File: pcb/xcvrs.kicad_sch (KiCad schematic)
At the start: 6 parts, among them U6 TCAN3403-Q1

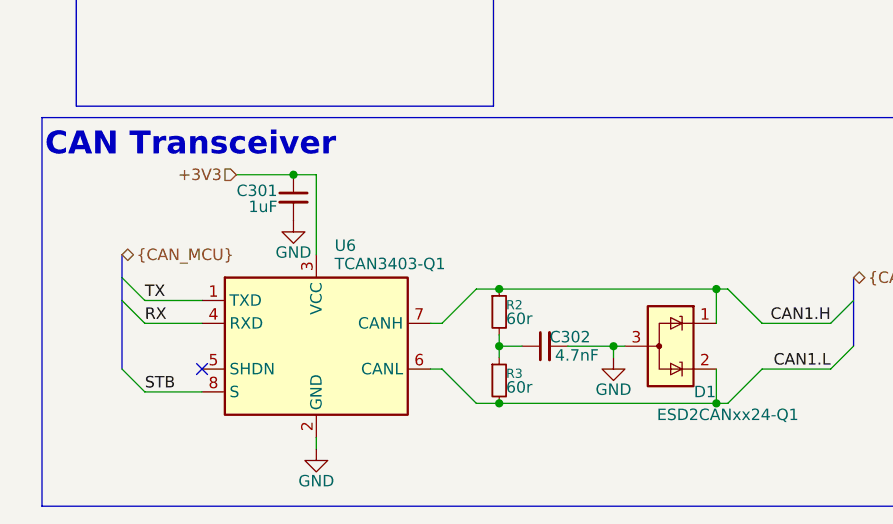
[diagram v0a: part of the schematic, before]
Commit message: pcb gitignore update, netting and mcu pinning
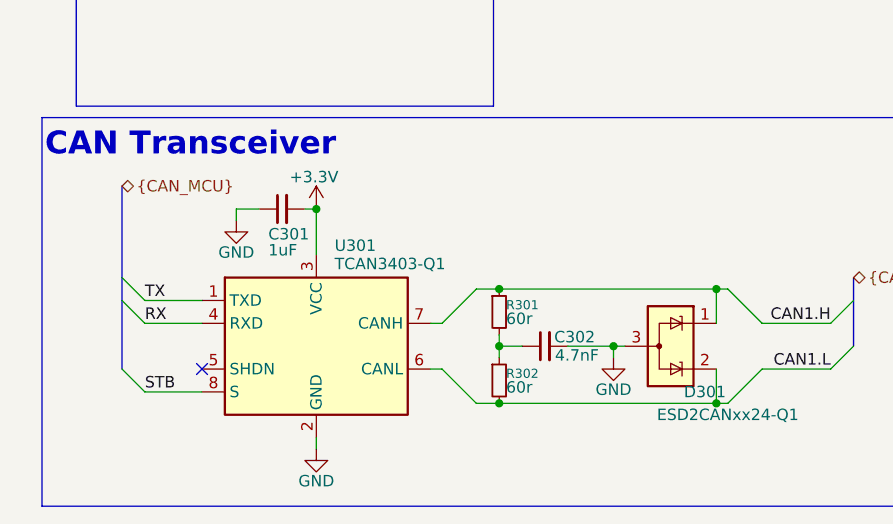
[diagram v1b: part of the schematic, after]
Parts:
- C301: footprint (none) -> Capacitor_SMD:C_0402_1005Metric
- R301: renamed from R2; footprint (none) -> Resistor_SMD:R_0402_1005Metric
- R302: renamed from R3; footprint (none) -> Resistor_SMD:R_0402_1005Metric
- renumbered D1 to D301, U6 to U301
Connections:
- net GND: now also C301.1; no longer C301.2
- net +3V3 renamed +3.3V
- net +3.3V: now also C301.2; no longer C301.1
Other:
- moved on the sheet: C301
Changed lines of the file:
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@@
+	)
+	(junction
+		(at 46.99 82.55)
+		(diameter 0)
+		(color 0 0 0 0)
 	)
 	(junction
@@
 	)
 	(junction
-		(at 44.45 78.74)
-		(diameter 0)
-		(color 0 0 0 0)
-	)
-	(junction
 		(at 80.01 97.79)
 		(diameter 0)
@@
 	(wire
 		(pts
-			(xy 46.99 78.74) (xy 46.99 87.63)
-		)
-		(stroke
-			(width 0)
-			(type default)
-		)
-	)
-	(wire
-		(pts
 			(xy 88.9 33.02) (xy 100.33 33.02)
 		)
@@
 	(wire
 		(pts
-			(xy 44.45 78.74) (xy 46.99 78.74)
-		)
-		(stroke
-			(width 0)
-			(type default)
-		)
-	)
-	(wire
-		(pts
 			(xy 91.44 91.44) (xy 92.71 91.44)
 		)
@@
 	(wire
 		(pts
+			(xy 46.99 82.55) (xy 46.99 87.63)
+		)
+		(stroke
+			(width 0)
+			(type default)
+		)
+	)
+	(wire
+		(pts
 			(xy 46.99 107.95) (xy 46.99 109.22)
 		)
@@
 	(wire
 		(pts
+			(xy 45.72 82.55) (xy 46.99 82.55)
+		)
+		(stroke
+			(width 0)
+			(type default)
+		)
+	)
+	(wire
+		(pts
 			(xy 105.41 48.26) (xy 81.28 48.26)
 		)
@@
 		)
 	)
+	(wire
+		(pts
+			(xy 38.1 82.55) (xy 40.64 82.55)
+		)
+		(stroke
+			(width 0)
+			(type default)
+		)
+	)
 	(bus
 		(pts
@@
 	(wire
 		(pts
-			(xy 38.1 78.74) (xy 44.45 78.74)
-		)
-		(stroke
-			(width 0)
-			(type default)
-		)
-	)
-	(wire
-		(pts
 			(xy 96.52 95.25) (xy 92.71 91.44)
 		)
@@
 	(wire
 		(pts
+			(xy 38.1 82.55) (xy 38.1 83.82)
+		)
+		(stroke
+			(width 0)
+			(type default)
+		)
+	)
+	(wire
+		(pts
 			(xy 81.28 97.79) (xy 80.01 97.79)
 		)
@@
 	(bus
 		(pts
-			(xy 25.4 87.63) (xy 25.4 90.17)
+			(xy 25.4 80.01) (xy 25.4 90.17)
 		)
 		(stroke
@@
 			)
 			(justify left bottom)
-		)
-	)
-	(hierarchical_label "+3V3"
-		(shape input)
-		(at 38.1 78.74 180)
-		(effects
-			(font
-				(size 1.27 1.27)
-			)
-			(justify right)
 		)
 	)
@@
 	(hierarchical_label "{CAN_MCU}"
 		(shape bidirectional)
-		(at 25.4 87.63 0)
+		(at 25.4 80.01 0)
 		(effects
 			(font
@@
 			)
 			(justify left)
+		)
+	)
+	(symbol
+		(lib_id "power:+BATT")
+		(at 46.99 82.55 0)
+		(unit 1)
+		(exclude_from_sim no)
+		(in_bom yes)
+		(on_board yes)
+		(dnp no)
+		(property "Reference" "#PWR026"
+			(at 46.99 86.36 0)
+			(effects
+				(font
+					(size 1.27 1.27)
+				)
+				(hide yes)
+			)
+		)
+		(property "Value" "+3.3V"
+			(at 46.736 78.994 0)
+			(effects
+				(font
+					(size 1.27 1.27)
+				)
+			)
+		)
+		(property "Footprint" ""
+			(at 46.99 82.55 0)
+			(effects
+				(font
+					(size 1.27 1.27)
+				)
+				(hide yes)
+			)
+		)
+		(property "Datasheet" ""
+			(at 46.99 82.55 0)
+			(effects
+				(font
+					(size 1.27 1.27)
+				)
+				(hide yes)
+			)
+		)
+		(property "Description" "Power symbol creates a global label with name \"+BATT\""
+			(at 46.99 82.55 0)
+			(effects
+				(font
+					(size 1.27 1.27)
+				)
+				(hide yes)
+			)
+		)
+		(pin "1"
+		)
+		(instances
+			(project "kh_obd2_interface"
+				(path "/0736e313-8db4-41af-b70d-53af7104d2ca/5885c24f-1a9e-44c2-aba7-d9491c98e256"
+					(reference "#PWR026")
+					(unit 1)
+				)
+			)
 		)
 	)
@@
 		(dnp no)
 		(property "Reference" "C302"
-			(at 75.184 96.774 90)
+			(at 75.692 96.774 90)
 			(effects
 				(font
@@
 		(on_board yes)
 		(dnp no)
-		(property "Reference" "R3"
+		(property "Reference" "R302"
 			(at 68.072 100.838 0)
 			(effects
@@
 			)
 		)
-		(property "Footprint" ""
+		(property "Footprint" "Resistor_SMD:R_0402_1005Metric"
 			(at 67.31 101.6 0)
 			(effects
@@
 			(project "kh_obd2_interface"
 				(path "/0736e313-8db4-41af-b70d-53af7104d2ca/5885c24f-1a9e-44c2-aba7-d9491c98e256"
-					(reference "R3")
+					(reference "R302")
 					(unit 1)
 				)
@@
 	(symbol
 		(lib_id "power:GND")
-		(at 44.45 83.82 0)
+		(at 38.1 83.82 0)
 		(unit 1)
 		(exclude_from_sim no)
@@
 		(dnp no)
 		(property "Reference" "#PWR011"
-			(at 44.45 90.17 0)
+			(at 38.1 90.17 0)
 			(effects
 				(font
@@
 		)
 		(property "Value" "GND"
-			(at 44.45 87.376 0)
+			(at 38.1 87.376 0)
 			(effects
 				(font
@@
 		)
 		(property "Footprint" ""
-			(at 44.45 83.82 0)
+			(at 38.1 83.82 0)
 			(effects
 				(font
@@
 		)
 		(property "Datasheet" ""
-			(at 44.45 83.82 0)
+			(at 38.1 83.82 0)
 			(effects
 				(font
@@
 		)
 		(property "Description" "Power symbol creates a global label with name \"GND\" , ground"
-			(at 44.45 83.82 0)
+			(at 38.1 83.82 0)
 			(effects
 				(font
@@
 	(symbol
 		(lib_id "Device:C_Small")
-		(at 44.45 81.28 0)
+		(at 43.18 82.55 90)
 		(unit 1)
 		(exclude_from_sim no)
@@
 		(dnp no)
 		(property "Reference" "C301"
-			(at 42.672 80.518 0)
+			(at 41.656 85.344 90)
 			(effects
 				(font
@@
 		)
 		(property "Value" "1uF"
-			(at 42.672 82.296 0)
+			(at 41.656 87.122 90)
 			(effects
 				(font
@@
 			)
 		)
-		(property "Footprint" ""
-			(at 44.45 81.28 0)
+		(property "Footprint" "Capacitor_SMD:C_0402_1005Metric"
+			(at 43.18 82.55 0)
 			(effects
 				(font
@@
 		)
 		(property "Datasheet" "~"
-			(at 44.45 81.28 0)
+			(at 43.18 82.55 0)
 			(effects
 				(font
@@
 		)
 		(property "Description" "Unpolarized capacitor, small symbol"
-			(at 44.45 81.28 0)
+			(at 43.18 82.55 0)
 			(effects
 				(font
@@
 		(on_board yes)
 		(dnp no)
-		(property "Reference" "R2"
+		(property "Reference" "R301"
 			(at 68.072 93.218 0)
 			(effects
@@
 			)
 		)
-		(property "Footprint" ""
+		(property "Footprint" "Resistor_SMD:R_0402_1005Metric"
 			(at 67.31 93.98 0)
 			(effects
@@
 			(project ""
 				(path "/0736e313-8db4-41af-b70d-53af7104d2ca/5885c24f-1a9e-44c2-aba7-d9491c98e256"
-					(reference "R2")
+					(reference "R301")
 					(unit 1)
 				)
@@
 		(on_board yes)
 		(dnp no)
-		(property "Reference" "U6"
+		(property "Reference" "U301"
 			(at 49.022 86.614 0)
 			(effects
@@
 			(project ""
 				(path "/0736e313-8db4-41af-b70d-53af7104d2ca/5885c24f-1a9e-44c2-aba7-d9491c98e256"
-					(reference "U6")
+					(reference "U301")
 					(unit 1)
 				)
@@
 		(on_board yes)
 		(dnp no)
-		(property "Reference" "D1"
+		(property "Reference" "D301"
 			(at 90.17 102.87 90)
 			(effects
@@
 			(project ""
 				(path "/0736e313-8db4-41af-b70d-53af7104d2ca/5885c24f-1a9e-44c2-aba7-d9491c98e256"
-					(reference "D1")
+					(reference "D301")
 					(unit 1)
 				)

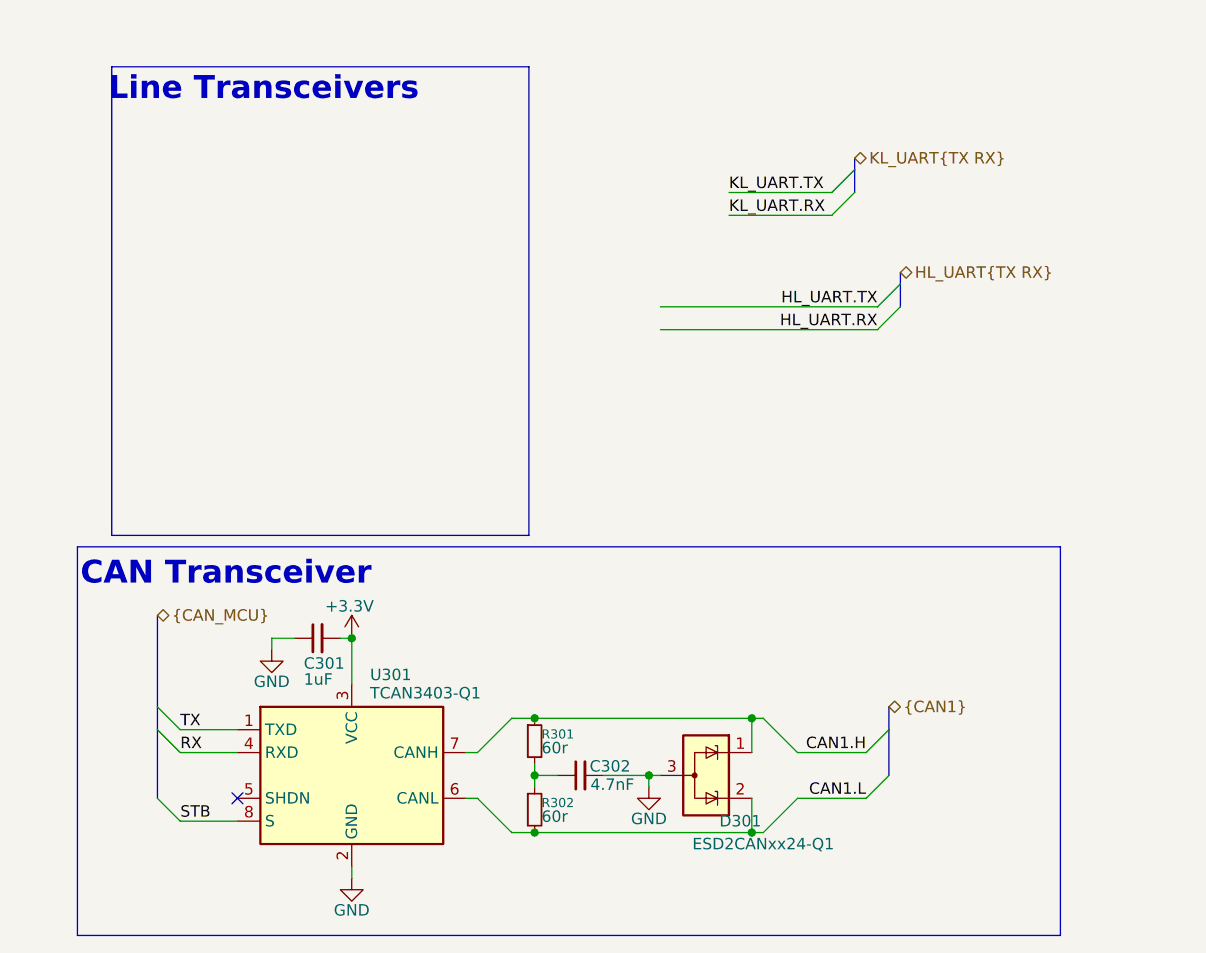
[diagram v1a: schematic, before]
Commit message: add transceivers, routing, drc
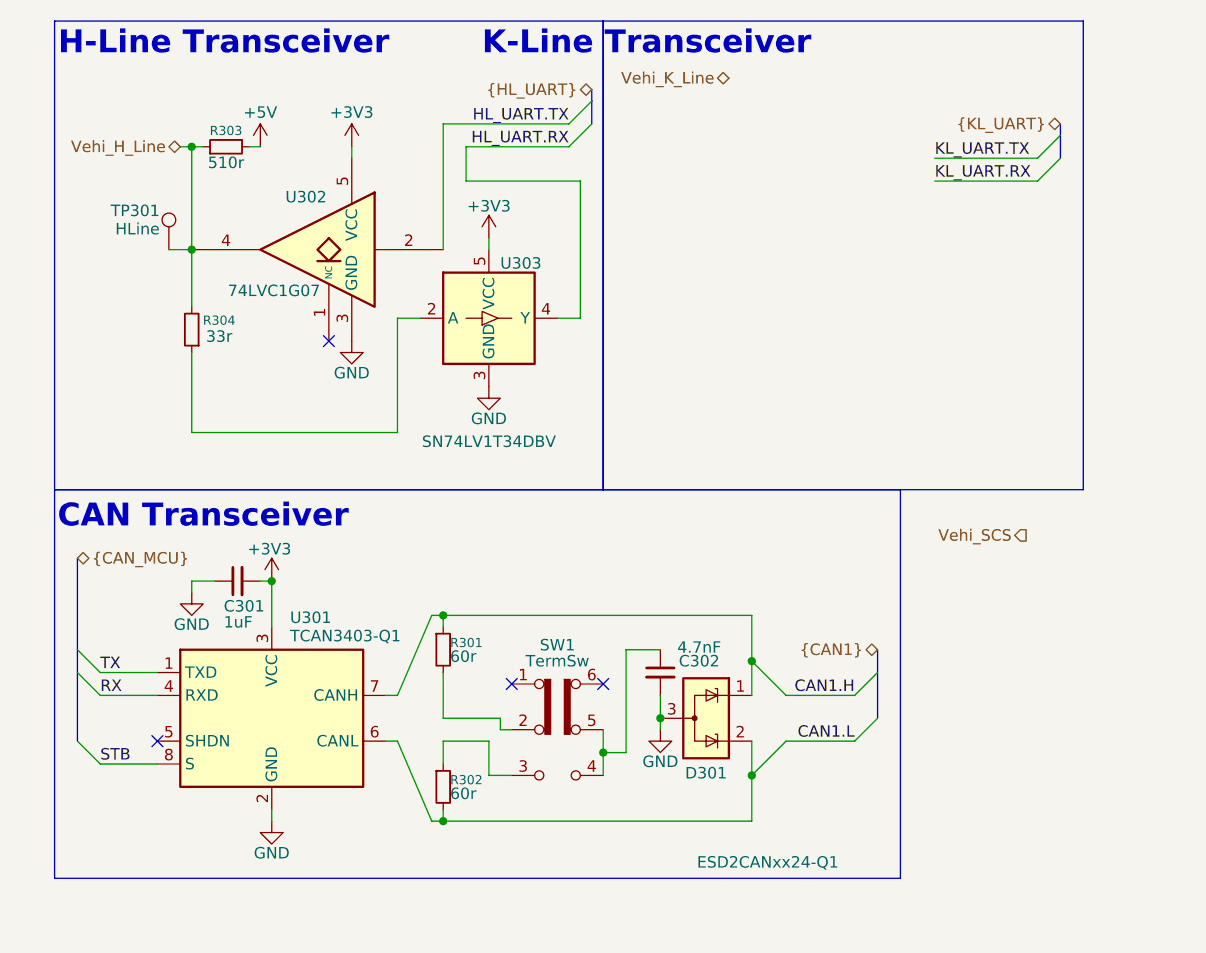
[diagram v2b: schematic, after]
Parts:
- added R303: 510r, Resistor_SMD:R_0402_1005Metric, symbol Device:R_Small
- added R304: 33r, Resistor_SMD:R_0402_1005Metric, symbol Device:R_Small
- added SW1: TermSw, Button_Switch_SMD:SW_DPDT_CK_JS202011JCQN, symbol Switch:SW_Slide_DPDT
- added TP301: HLine, TestPoint:TestPoint_Pad_D1.0mm, symbol Connector:TestPoint
- added U302: 74LVC1G07, Package_TO_SOT_SMD:Texas_R-PDSO-G5_DCK-5, symbol 74xGxx:74LVC1G07
- added U303: SN74LV1T34DBV, Package_TO_SOT_SMD:SOT-23-5, symbol Logic_LevelTranslator:SN74LV1T34DBV
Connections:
- net GND: now also U302.3 (GND), U303.3 (GND)
- net HL_UART.RX: now also U303.4 (Y)
- net HL_UART.TX: now also U302.2
- net +3.3V renamed +3V3
- net +3V3: now also U302.5 (VCC), U303.5 (VCC)
- new net: R301.2, SW1.2 (B)
- new net: R302.1, SW1.3 (C)
- new net: C302.1, SW1.4 (A), SW1.5 (B)
- new net: R304.1, U303.2 (A)
- new net +5V: R303.2
- new net Vehi_H_Line: R303.1, R304.2, TP301.1, U302.4
- no-connect marks 1 -> 4
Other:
- note added: "H-Line Transceiver"
- note added: "K-Line Transceiver"
- note removed: "Line Transceivers"
- moved on the sheet: C301, C302, D301, R301, R302, U301

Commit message: busses are hard
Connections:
- net CAN1.H renamed H_+
- net CAN1.L renamed L_-
- net HL_UART.RX renamed HLINE.RX
- net HL_UART.TX renamed HLINE.TX

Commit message: Add TLIN2027, placement, DRC fixes, routing
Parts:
- removed SW1: TermSw, Button_Switch_SMD:SW_DPDT_CK_JS202011JCQN, symbol Switch:SW_Slide_DPDT
- added JP1, JP2: SolderJumper_2_Open, Jumper:SolderJumper-2_P1.3mm_Open_RoundedPad1.0x1.5mm, symbol Jumper:SolderJumper_2_Open
- added R305: 5.1k, Resistor_SMD:R_0402_1005Metric, symbol Device:R_Small
- added U2: TLIN2027-Q1, Package_SO:SOIC-8_3.9x4.9mm_P1.27mm, symbol TIParts:TLIN2027DRQ1
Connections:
- net +3V3: now also R305.1
- net GND: now also U2.5 (GND)
- net H_+: now also JP1.1 (A); no longer R301.1
- net KLINE.RX: now also U2.1 (RXD)
- net KLINE.TX: now also U2.4 (TXD)
- net L_-: now also JP2.2 (B); no longer R302.2
- net Vehi_K_Line: now also U2.6 (LIN)
- net at R301.2: now also C302.1, R302.1
- new net: JP2.1 (A), R302.2
- new net: JP1.2 (B), R301.1
- new net: R305.2, U2.2 (~{EN})
- no-connect marks 4 -> 2
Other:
- moved on the sheet: C302, R301, R302

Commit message: CAN/mcu placement/routing
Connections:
- net +12V: now reaches U2.7 (VBAT)
- net H_+ renamed CAN.P
- net L_- renamed CAN.N
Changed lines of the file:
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@@
 	(paper "A4")
 	(bus_alias "CAN"
-		(members "H_+" "L_-")
+		(members "P" "N")
 	)
 	(bus_alias "CAN_MCU"
@@
 		)
 	)
-	(label "L_-"
-		(at 99.06 93.98 0)
+	(label "CAN.N"
+		(at 102.87 93.98 180)
 		(effects
 			(font
 				(size 1.27 1.27)
 			)
-			(justify left bottom)
+			(justify right bottom)
 		)
 	)
@@
 		)
 	)
-	(label "H_+"
-		(at 99.06 88.9 0)
+	(label "CAN.P"
+		(at 102.87 88.9 180)
 		(effects
 			(font
 				(size 1.27 1.27)
 			)
-			(justify left bottom)
+			(justify right bottom)
 		)
 	)
@@
 		)
 	)
-	(hierarchical_label "{CAN}"
+	(hierarchical_label "CAN{CAN}"
 		(shape bidirectional)
 		(at 105.41 83.82 180)
@@
 		(dnp no)
 		(property "Reference" "C302"
-			(at 77.47 89.154 90)
+			(at 77.47 88.9 90)
 			(effects
 				(font
@@
 		)
 		(property "Value" "4.7nF"
-			(at 77.47 87.376 90)
+			(at 77.47 87.122 90)
 			(effects
 				(font
@@
 					(unit 1)
 				)
+			)
+		)
+	)
+	(symbol
+		(lib_id "power:+BATT")
+		(at 101.6 34.29 0)
+		(unit 1)
+		(exclude_from_sim no)
+		(in_bom yes)
+		(on_board yes)
+		(dnp no)
+		(property "Reference" "#PWR040"
+			(at 101.6 38.1 0)
+			(effects
+				(font
+					(size 1.27 1.27)
+				)
+				(hide yes)
+			)
+		)
+		(property "Value" "+12V"
+			(at 101.346 30.734 0)
+			(effects
+				(font
+					(size 1.27 1.27)
+				)
+			)
+		)
+		(property "Footprint" ""
+			(at 101.6 34.29 0)
+			(effects
+				(font
+					(size 1.27 1.27)
+				)
+				(hide yes)
+			)
+		)
+		(property "Datasheet" ""
+			(at 101.6 34.29 0)
+			(effects
+				(font
+					(size 1.27 1.27)
+				)
+				(hide yes)
+			)
+		)
+		(property "Description" "Power symbol creates a global label with name \"+BATT\""
+			(at 101.6 34.29 0)
+			(effects
+				(font
+					(size 1.27 1.27)
+				)
+				(hide yes)
+			)
+		)
+		(pin "1"
+		)
+		(instances
+			(project "kh_obd2_interface"
+				(path "/0736e313-8db4-41af-b70d-53af7104d2ca/5885c24f-1a9e-44c2-aba7-d9491c98e256"
+					(reference "#PWR040")
+					(unit 1)
+				)

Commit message: status/info leds, extra 5v cap
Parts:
- removed TP301: HLine, TestPoint:TestPoint_Pad_D1.0mm, symbol Connector:TestPoint
- renumbered U2 to U304
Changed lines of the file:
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@@
-	(wire
-		(pts
-			(xy 26.67 39.37) (xy 29.21 39.37)
-		)
-		(stroke
-			(width 0)
-			(type default)
-		)
-	)
 	(wire
 		(pts
@@
 	)
 	(symbol
-		(lib_id "Connector:TestPoint")
-		(at 26.67 39.37 0)
-		(unit 1)
-		(exclude_from_sim no)
-		(in_bom yes)
-		(on_board yes)
-		(dnp no)
-		(property "Reference" "TP301"
-			(at 25.654 35.052 0)
-			(effects
-				(font
-					(size 1.27 1.27)
-				)
-				(justify right)
-			)
-		)
-		(property "Value" "HLine"
-			(at 25.654 37.084 0)
-			(effects
-				(font
-					(size 1.27 1.27)
-				)
-				(justify right)
-			)
-		)
-		(property "Footprint" "TestPoint:TestPoint_Pad_D1.0mm"
-			(at 31.75 39.37 0)
-			(effects
-				(font
-					(size 1.27 1.27)
-				)
-				(hide yes)
-			)
-		)
-		(property "Datasheet" "~"
-			(at 31.75 39.37 0)
-			(effects
-				(font
-					(size 1.27 1.27)
-				)
-				(hide yes)
-			)
-		)
-		(property "Description" "test point"
-			(at 26.67 39.37 0)
-			(effects
-				(font
-					(size 1.27 1.27)
-				)
-				(hide yes)
-			)
-		)
-		(pin "1"
-		)
-		(instances
-			(project ""
-				(path "/0736e313-8db4-41af-b70d-53af7104d2ca/5885c24f-1a9e-44c2-aba7-d9491c98e256"
-					(reference "TP301")
-					(unit 1)
-				)
-			)
-		)
-	)
-	(symbol
 		(lib_id "power:GND")
 		(at 38.1 102.87 0)
@@
 		(on_board yes)
 		(dnp no)
-		(property "Reference" "U2"
+		(property "Reference" "U304"
 			(at 103.886 33.782 0)
 			(effects
@@
 			(project ""
 				(path "/0736e313-8db4-41af-b70d-53af7104d2ca/5885c24f-1a9e-44c2-aba7-d9491c98e256"
-					(reference "U2")
-					(unit 1)
-				)
+					(reference "U304")
+					(unit 1)
+				)

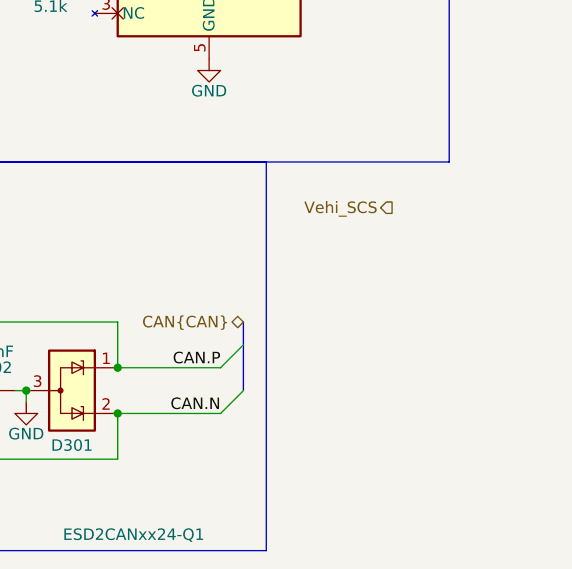
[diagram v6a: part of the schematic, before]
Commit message: dbg uart, nrst, SCS drive, etc
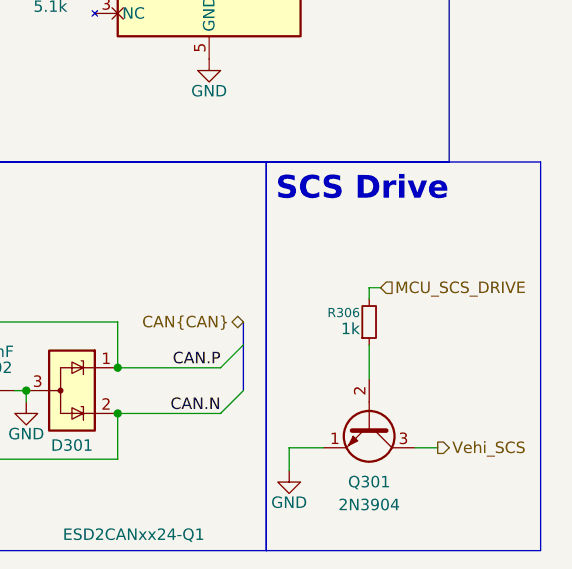
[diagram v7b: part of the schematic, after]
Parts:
- added Q301: 2N3904, Package_TO_SOT_SMD:SOT-23, symbol Transistor_BJT:2N3904
- added R306: 1k, Resistor_SMD:R_0402_1005Metric, symbol Device:R_Small
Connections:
- net GND: now also Q301.1 (E)
- net Vehi_SCS: now also Q301.3 (C)
- new net: Q301.2 (B), R306.1
- new net MCU_SCS_DRIVE: R306.2
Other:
- note added: "SCS Drive"

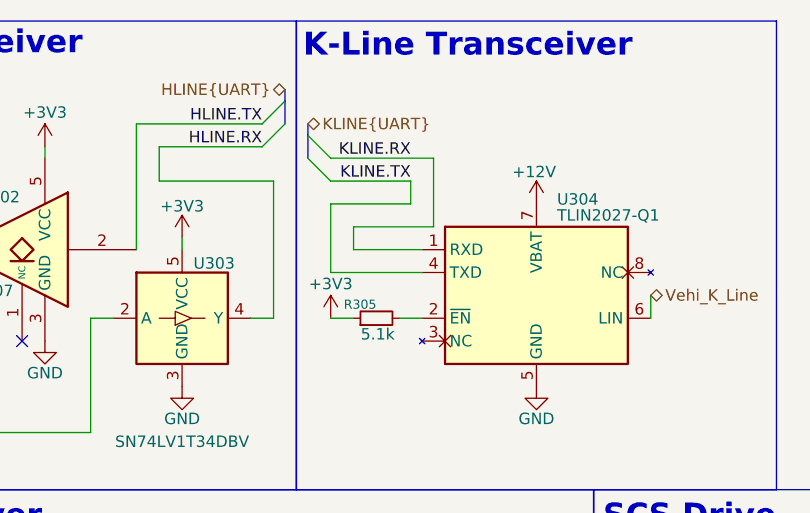
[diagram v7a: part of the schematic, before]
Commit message: led dout testpoint
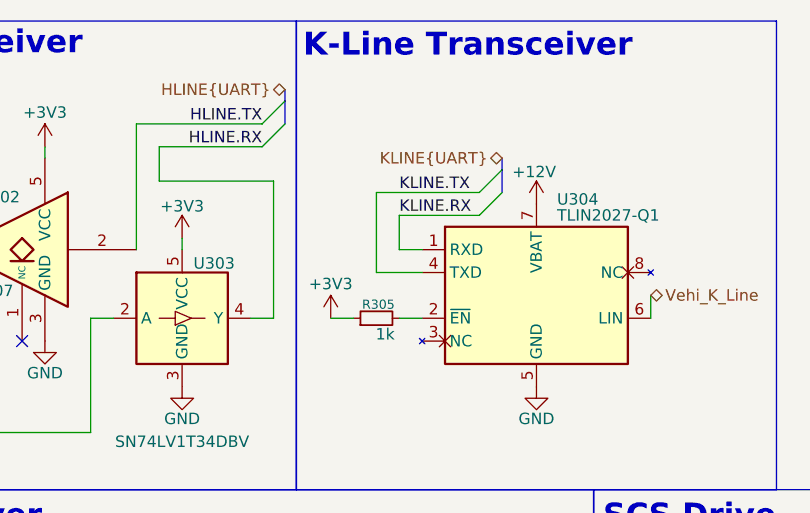
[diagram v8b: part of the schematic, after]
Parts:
- R305: value 5.1k -> 1k
